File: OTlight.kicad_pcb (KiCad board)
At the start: 2 copper layers, 68 parts, among them P1 CONN_01X01, Q1 TEMT6000, Q2 Q_NMOS_GSD, T1 TRANSFO, U1 LM3478, U10 IN-14, U11 IN-14, U12 MAX6931, U13 IN-14, U14 MAX6920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

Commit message: Misakaimouto Silk + miniBiri stitch
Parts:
- removed the G*** at (47.2, 111.8)
- added G***: LOGO, OTlight:Misakaimouto, F.Cu at (47.2, 111.8)
- added REF**: Biri-Biri via, BamboulabFootprints:Biri-Biri-via-small, F.Cu at (51.8, 113.3)
- added REF**: Biri-Biri via, BamboulabFootprints:Biri-Biri-via-small, F.Cu at (89.2, 104.3)
- added REF**: Biri-Biri via, BamboulabFootprints:Biri-Biri-via-small, F.Cu at (86.4, 129.5)
- added REF**: Biri-Biri via, BamboulabFootprints:Biri-Biri-via-small, F.Cu at (91.3, 86.5)
- added REF**: Biri-Biri via, BamboulabFootprints:Biri-Biri-via-small, F.Cu at (121.3, 104.3)
- added REF**: Biri-Biri via, BamboulabFootprints:Biri-Biri-via-small, F.Cu at (118.7, 115.3)
- added REF**: Biri-Biri via, BamboulabFootprints:Biri-Biri-via-small, F.Cu at (116.6, 98.7)
- added REF**: Biri-Biri via, BamboulabFootprints:Biri-Biri-via-small, F.Cu at (60.8, 126.1)
- added REF**: Biri-Biri via, BamboulabFootprints:Biri-Biri-via-small, F.Cu at (79.0, 86.7)
- added REF**: Biri-Biri via, BamboulabFootprints:Biri-Biri-via-small, F.Cu at (57.4, 104.1)
- added REF**: Biri-Biri via, BamboulabFootprints:Biri-Biri-via-small, F.Cu at (103.4, 81.9)

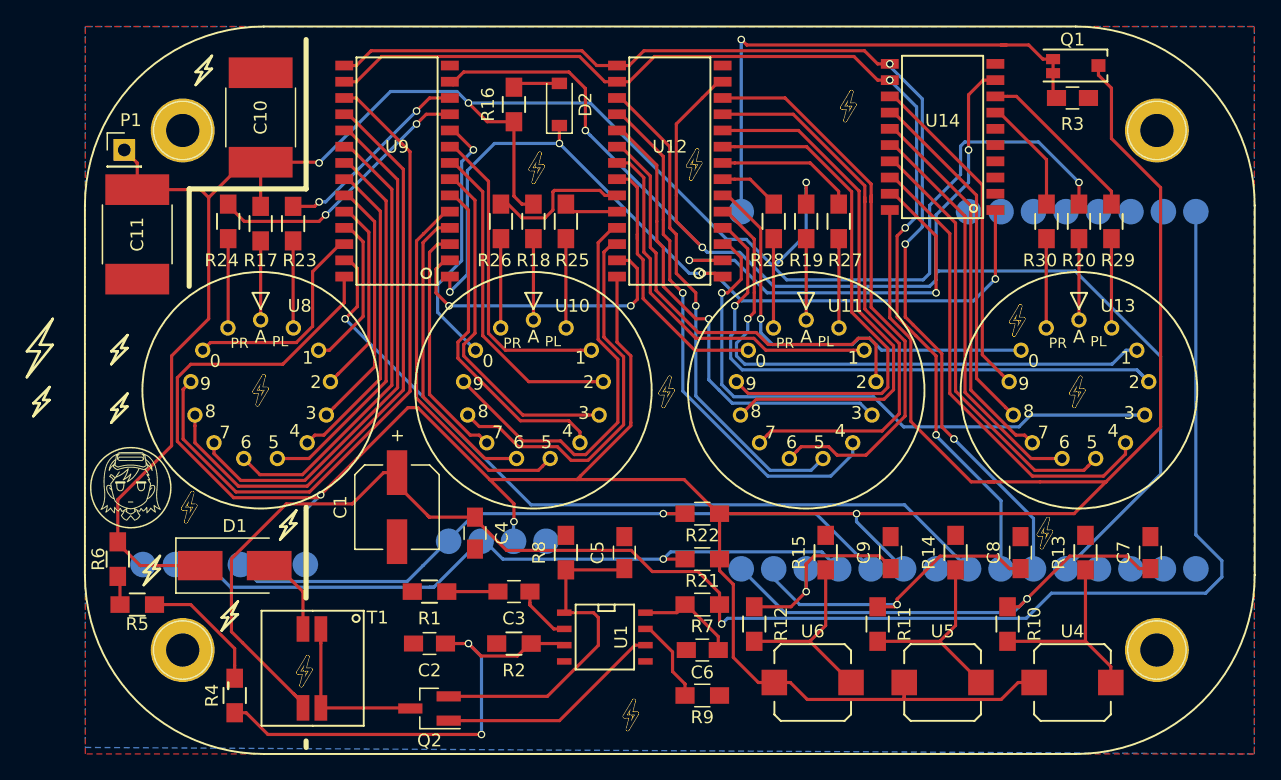
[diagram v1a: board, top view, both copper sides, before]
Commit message: Added Edgecut on top of the Altoids silkscreen
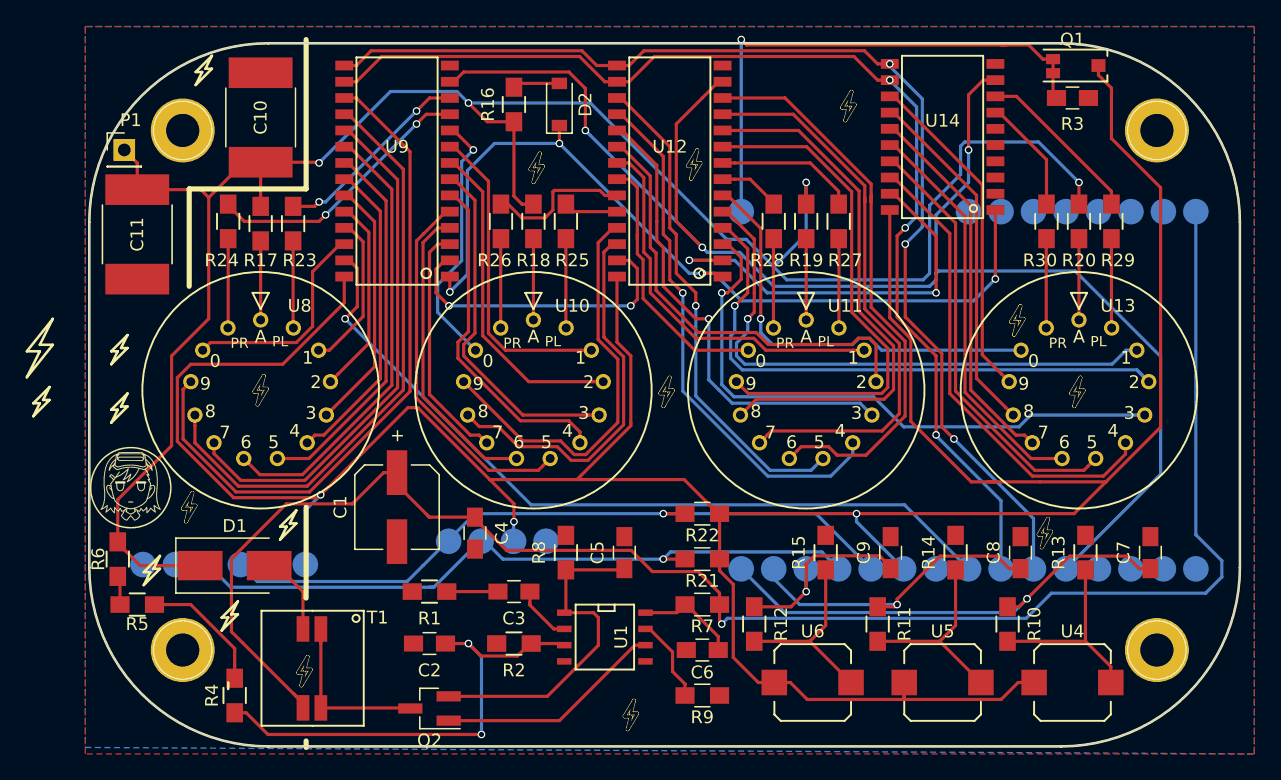
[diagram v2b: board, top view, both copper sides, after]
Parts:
- removed the REF** at (89.4, 104.1)
- moved ? 0.43 mm to (89.0, 104.0)
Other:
- board outline added: 90 x 55 mm
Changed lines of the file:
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@@
-(kicad_pcb (version 4) (host pcbnew 4.0.5)
+(kicad_pcb (version 4) (host pcbnew 4.0.6)
   (general
-    (links 0)
-    (no_connects 31)
+    (links 235)
+    (no_connects 97)
     (area 39.015999 74.51657 135.911001 132.865001)
     (thickness 1.6)
-    (drawings 57)
+    (drawings 65)
     (tracks 859)
     (zones 0)
-    (modules 79)
+    (modules 78)
     (nets 105)
   )
@@
     )
   )
-  (module BamboulabFootprints:Altoid (layer B.Cu)
-    (at 89.408 104.14)
-    (fp_text reference REF** (at 0 -5.08) (layer B.SilkS) hide
-      (effects (font (size 1 1) (thickness 0.15)) (justify mirror))
-    )
-    (fp_text value Altoid (at 0 5.08) (layer B.Fab)
-      (effects (font (size 1 1) (thickness 0.15)) (justify mirror))
-    )
-    (fp_line (start -31.75 28.45) (end 31.75 28.45) (layer B.SilkS) (width 0.15))
-    (fp_line (start -45.75 14.45) (end -45.75 -14.45) (layer B.SilkS) (width 0.15))
-    (fp_arc (start -31.75 14.45) (end -45.75 14.45) (angle -90) (layer B.SilkS) (width 0.15))
-    (fp_arc (start -31.75 -14.45) (end -45.75 -14.45) (angle 90) (layer B.SilkS) (width 0.15))
-    (fp_line (start 45.75 14.45) (end 45.75 -14.45) (layer B.SilkS) (width 0.15))
-    (fp_line (start -31.75 -28.45) (end 31.75 -28.45) (layer B.SilkS) (width 0.15))
-    (fp_arc (start 31.75 14.45) (end 31.75 28.45) (angle -90) (layer B.SilkS) (width 0.15))
-    (fp_arc (start 31.75 -14.45) (end 45.75 -14.45) (angle -90) (layer B.SilkS) (width 0.15))
-  )
-  (module BamboulabFootprints:Altoid (layer F.Cu)
-    (at 89.408 104.14)
-    (fp_text reference "" (at 0 5.08) (layer F.SilkS)
-      (effects (font (size 1 1) (thickness 0.15)))
-    )
-    (fp_text value Altoid (at 0 -5.08) (layer F.Fab)
-      (effects (font (size 1 1) (thickness 0.15)))
-    )
-    (fp_line (start -31.75 -28.45) (end 31.75 -28.45) (layer F.SilkS) (width 0.15))
-    (fp_line (start -45.75 -14.45) (end -45.75 14.45) (layer F.SilkS) (width 0.15))
-    (fp_arc (start -31.75 -14.45) (end -45.75 -14.45) (angle 90) (layer F.SilkS) (width 0.15))
-    (fp_arc (start -31.75 14.45) (end -45.75 14.45) (angle -90) (layer F.SilkS) (width 0.15))
-    (fp_line (start 45.75 -14.45) (end 45.75 14.45) (layer F.SilkS) (width 0.15))
-    (fp_line (start -31.75 28.45) (end 31.75 28.45) (layer F.SilkS) (width 0.15))
-    (fp_arc (start 31.75 -14.45) (end 31.75 -28.45) (angle 90) (layer F.SilkS) (width 0.15))
-    (fp_arc (start 31.75 14.45) (end 45.75 14.45) (angle 90) (layer F.SilkS) (width 0.15))
-  )
   (module BamboulabFootprints:SPEH120100 (layer F.Cu)
     (at 120.904 127 180)
@@
       (net 2 GND) (zone_connect 2))
   )
+  (module BamboulabFootprints:Altoid (layer F.Cu)
+    (at 89 104)
+    (fp_text reference "" (at 0 5.08) (layer F.SilkS)
+      (effects (font (size 1 1) (thickness 0.15)))
+    )
+    (fp_text value Altoid (at 0 -6) (layer F.Fab)
+      (effects (font (size 1 1) (thickness 0.15)))
+    )
+    (fp_arc (start 31 14) (end 45 14) (angle 90) (layer F.SilkS) (width 0.2))
+    (fp_line (start 45 -13) (end 45 14) (layer F.SilkS) (width 0.2))
+    (fp_line (start -31 28) (end 31 28) (layer F.SilkS) (width 0.2))
+    (fp_arc (start -31 14) (end -31 28) (angle 90) (layer F.SilkS) (width 0.2))
+    (fp_line (start -45 -13) (end -45 14) (layer F.SilkS) (width 0.2))
+    (fp_arc (start 31 -13) (end 31 -27) (angle 90) (layer F.SilkS) (width 0.2))
+    (fp_arc (start -31 -13) (end -45 -13) (angle 90) (layer F.SilkS) (width 0.2))
+    (fp_line (start -31 -27) (end 31 -27) (layer F.SilkS) (width 0.2))
+  )
+  (gr_arc (start 58 91) (end 44 91) (angle 90) (layer Edge.Cuts) (width 0.1))
+  (gr_arc (start 58 118) (end 58 132) (angle 90) (layer Edge.Cuts) (width 0.1))
+  (gr_arc (start 120 118) (end 134 118) (angle 90) (layer Edge.Cuts) (width 0.1))
+  (gr_arc (start 120 91) (end 120 77) (angle 90) (layer Edge.Cuts) (width 0.1))
+  (gr_line (start 134 118) (end 134 91) (layer Edge.Cuts) (width 0.1))
+  (gr_line (start 58 132) (end 120 132) (layer Edge.Cuts) (width 0.1))
+  (gr_line (start 44 91) (end 44 118) (layer Edge.Cuts) (width 0.1))
+  (gr_line (start 120 77) (end 58 77) (layer Edge.Cuts) (width 0.1))
   (gr_line (start 53.594 77.978) (end 53.086 78.994) (layer F.SilkS) (width 0.2))
   (gr_line (start 52.324 79.248) (end 53.594 77.978) (layer F.SilkS) (width 0.2))

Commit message: Board size to fit Altoids+ decoupling caps
NOTHING IS WHERE IT SHOULD BE
EVERYTHING IS WRONG
I AM GOING TO BED!
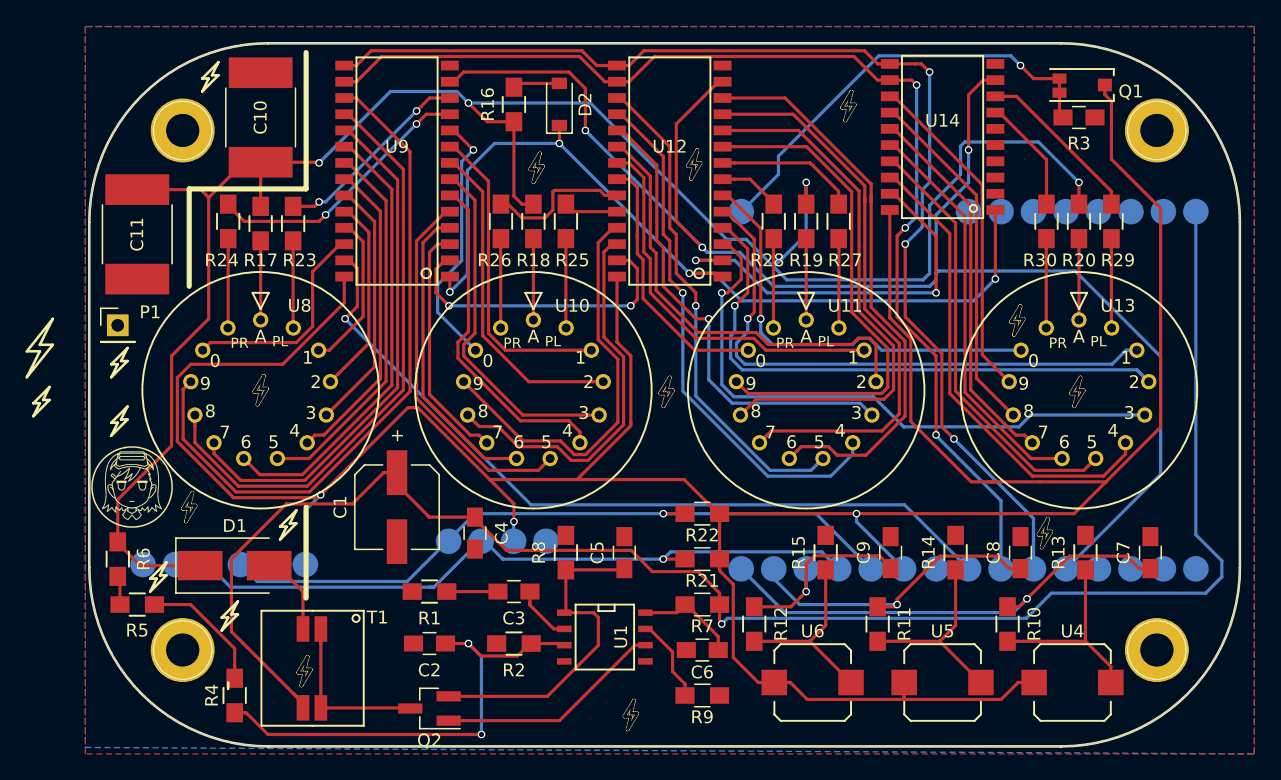
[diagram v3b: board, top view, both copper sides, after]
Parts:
- moved P1 13.7 mm to (46.2, 99.1)
- moved R3 1.61 mm to (121.4, 82.8)
- moved Q1 1.60 mm to (119.9, 80.3)
- moved G*** 0.11 mm to (47.3, 111.7)
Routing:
- net Net-(Q1-Pad2): track 42.1 -> 34.7 mm
- net /HVout: track 160.8 -> 157.3 mm
- net /CLK: track 90.1 -> 92.0 mm
- net +3V3: track 252.2 -> 250.4 mm
- net Net-(U12-Pad2): track 32.7 -> 31.7 mm
- net Net-(D2-Pad1): track 67.7 -> 68.8 mm
- net /LOAD: track 89.0 -> 90.0 mm

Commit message: Errr... as below but this time I saved first.
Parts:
- added C12: C_Small, Capacitors_SMD:C_0805_HandSoldering, F.Cu at (116.8, 90.9)
- added C13: C_Small, Capacitors_SMD:C_0805_HandSoldering, F.Cu at (80.8, 81.8)
- added C14: C_Small, Capacitors_SMD:C_0805_HandSoldering, F.Cu at (126.5, 90.9)
- added C15: C_Small, Capacitors_SMD:C_0805_HandSoldering, F.Cu at (110.7, 111.3)
- added C16: C_Small, Capacitors_SMD:C_0805_HandSoldering, F.Cu at (89.4, 111.3)
- moved D2 2.54 mm to (78.2, 81.8)
- moved R16 1.52 mm to (75.7, 81.8)
- moved REF** 0.64 mm to (79.0, 87.4)
- moved R17 0.17 mm to (57.4, 90.9)
- moved R23 0.17 mm to (59.9, 90.9)
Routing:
- net +3V3: track 250.4 -> 241.3 mm
- net Net-(C12-Pad2): track 68.8 -> 76.9 mm
- net Net-(R4-Pad1): track 10.0 -> 11.6 mm
- net Net-(D2-Pad2): track 3.68 -> 2.66 mm
- net /HVout: track 157.3 -> 156.4 mm

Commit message: Updated PCB and footprints - Changed footprints for angled pins SMD package - Repositioned holes - Locked Altoids shaped outline, holes, tubes and modules - Changed R3 for resistor package (was 0805 but as capacitor)
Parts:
- R3: footprint Capacitors_SMD:C_0805_HandSoldering -> Resistors_SMD:R_0805_HandSoldering
- U2: footprint BamboulabFootprints:NodeMCU-V2 -> BamboulabFootprints:NodeMCU-V3
- U3: footprint BamboulabFootprints:DS3231 -> BamboulabFootprints:DS3231-Angled
- U7: footprint BamboulabFootprints:BME280 -> BamboulabFootprints:BME280-Angled
- moved U7 5.18 mm to (54.9, 106.2)
- moved ? 2.59 mm to (127.0, 127.0)
- moved ? 2.56 mm to (51.0, 127.0)
- moved ? 1.89 mm to (127.0, 82.0)
- moved ? 1.85 mm to (51.0, 82.0)
- moved U2 0.79 mm to (112.0, 104.0)
- moved U3 0.44 mm to (75.7, 99.0)
- moved R3 0.10 mm to (121.5, 82.8)
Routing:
- net +5V: track 133.1 -> 63.0 mm, vias 1 -> 0
- net GND: track 2.76 -> 70.6 mm, vias 0 -> 1
- net Net-(C9-Pad1): track 16.1 -> 50.1 mm
- net /HVout: track 156.4 -> 134.7 mm, vias 4 -> 3
- net Net-(C8-Pad1): track 24.7 -> 8.04 mm, vias 1 -> 0
- net /BLANK: track 121.5 -> 106.8 mm, vias 3 -> 2
- net /CLK: track 92.0 -> 106.4 mm, vias 3 -> 4
- net Net-(C7-Pad1): track 37.7 -> 27.5 mm
- net Net-(U2-Pad12): track 0.00 -> 10.2 mm, vias 0 -> 1
- net +3V3: track 241.3 -> 246.2 mm, vias 3 -> 4
- net (no net): track 0.00 -> 2.03 mm

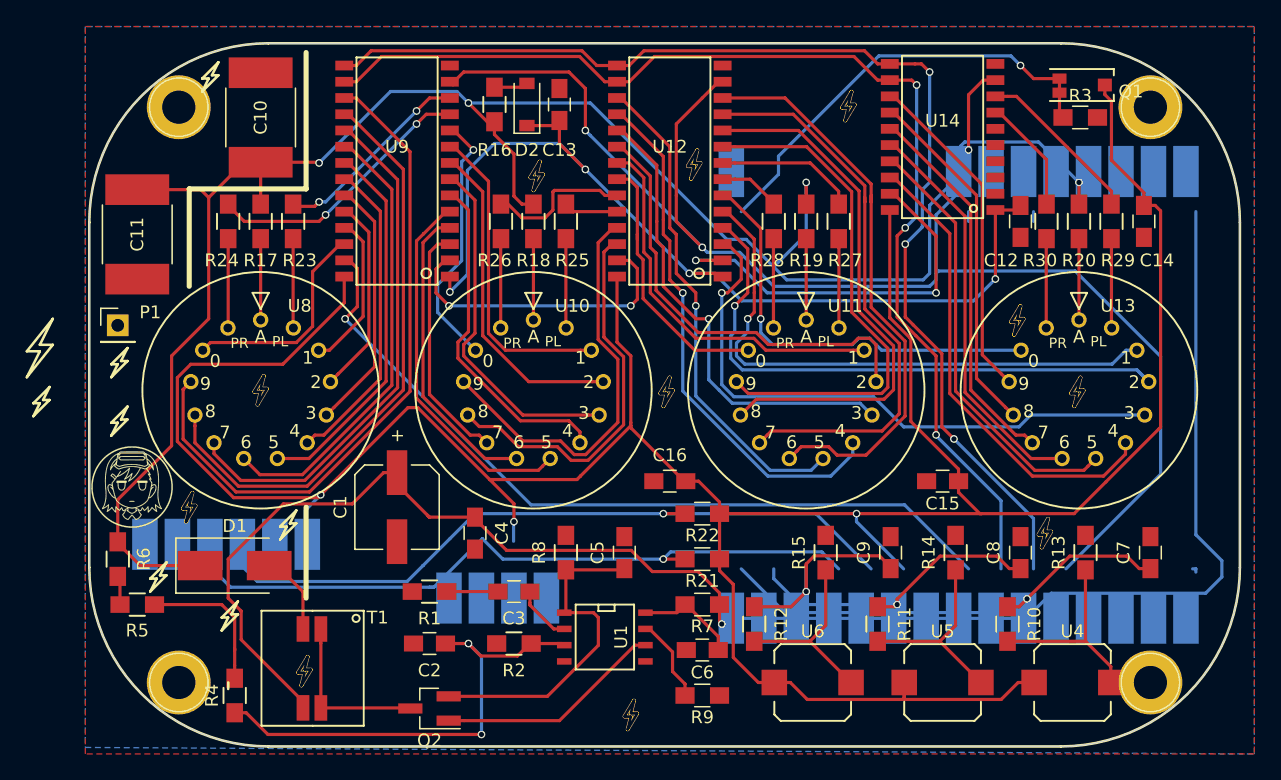
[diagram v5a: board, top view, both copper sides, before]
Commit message: Updated footprints meant reroute No unconnected traces, silk adjusted.
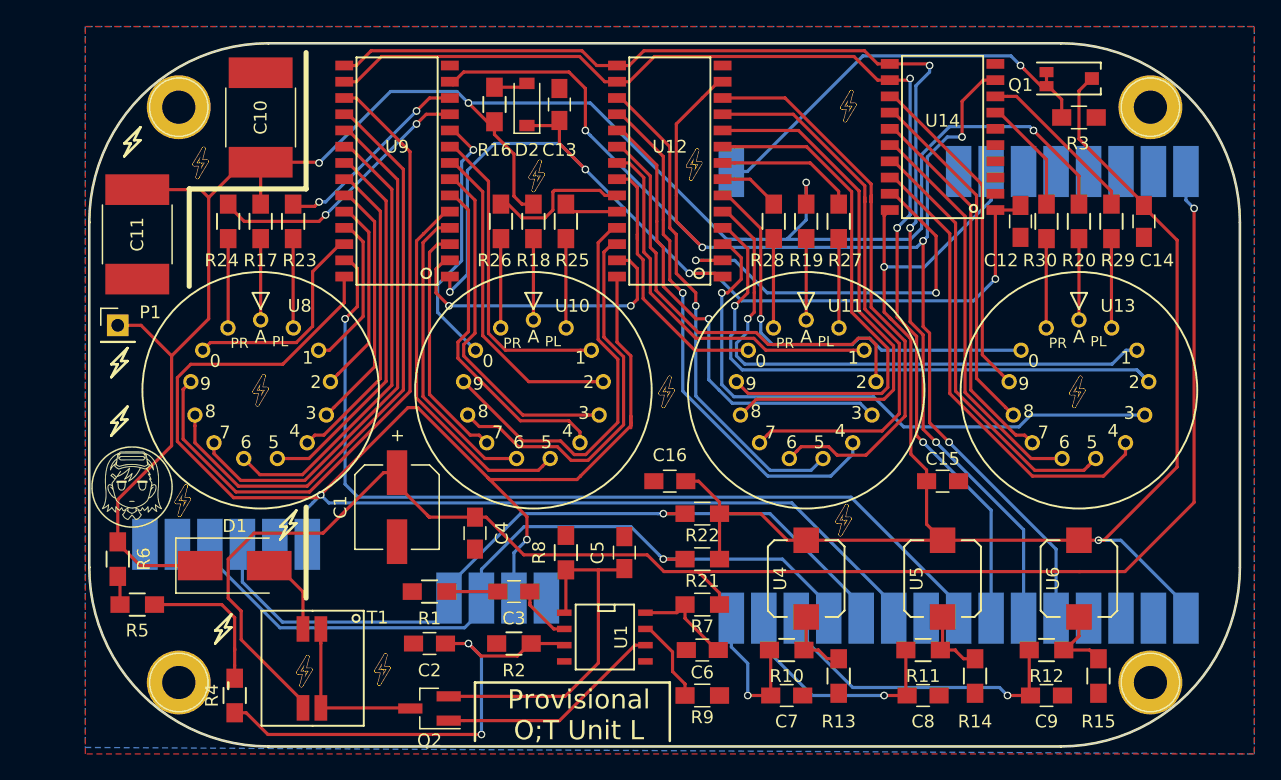
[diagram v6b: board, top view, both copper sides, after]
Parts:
- removed the REF** at (86.4, 129.5)
- removed the REF** at (118.7, 115.3)
- removed the REF** at (116.6, 98.7)
- added REF**: Biri-Biri via, BamboulabFootprints:Biri-Biri-via-small, F.Cu at (52.7, 86.4)
- added REF**: Biri-Biri via, BamboulabFootprints:Biri-Biri-via-small, F.Cu at (103.0, 114.3)
- added REF**: Biri-Biri via, BamboulabFootprints:Biri-Biri-via-small, F.Cu at (66.9, 126.0)
- moved C7 30.6 mm to (98.6, 128.0), turned to 0 degrees
- moved R15 23.4 mm to (122.9, 126.5), turned to 270 degrees
- moved R12 23.0 mm to (118.9, 124.5), turned to 0 degrees
- moved U4 22.4 mm to (100.1, 118.9), turned to 90 degrees
- moved U6 22.4 mm to (121.4, 118.9), turned to 90 degrees
- moved R13 21.6 mm to (102.6, 126.5), turned to 270 degrees
- moved R10 17.4 mm to (98.6, 124.5), turned to 0 degrees
- moved C9 16.5 mm to (118.9, 128.0), turned to 0 degrees
- moved C8 13.5 mm to (109.2, 128.0), turned to 0 degrees
- moved R14 9.77 mm to (113.3, 126.5), turned to 270 degrees
- moved U5 8.13 mm to (110.7, 118.9), turned to 90 degrees
- moved R11 4.10 mm to (109.2, 124.5), turned to 0 degrees
- moved Q1 1.14 mm to (118.9, 79.8)
- moved REF** 0.72 mm to (51.3, 112.8)
- moved R3 0.10 mm to (121.4, 82.8)
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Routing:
- net +5V: track 63.0 -> 131.0 mm, vias 0 -> 1
- net GND: track 70.6 -> 3.49 mm, vias 1 -> 0
- net +3V3: track 246.2 -> 278.8 mm
- net Net-(C9-Pad1): track 50.1 -> 25.0 mm
- net /HVout: track 134.7 -> 158.1 mm, vias 3 -> 4
- net Net-(C7-Pad1): track 27.5 -> 12.0 mm
- net Net-(C8-Pad1): track 8.04 -> 19.7 mm, vias 0 -> 1
- net /CLK: track 106.4 -> 95.6 mm, vias 4 -> 3
- net Net-(U2-Pad12): track 10.2 -> 0.00 mm, vias 1 -> 0
- net Net-(R10-Pad2): track 15.7 -> 5.66 mm
- net Net-(R11-Pad2): track 15.5 -> 5.69 mm
- net /DIN: track 62.5 -> 71.5 mm
- net Net-(R12-Pad2): track 15.0 -> 6.14 mm
- net Net-(R22-Pad2): track 55.6 -> 62.9 mm
- net Net-(R21-Pad2): track 55.3 -> 62.3 mm
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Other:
- board text added: "Provisional O;T Unit L"

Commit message: I2C footprint, silk and diode adjustments
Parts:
- P1: value CONN_01X01 -> CONN_01X02; footprint Socket_Strips:Socket_Strip_Straight_1x01_Pitch2.54mm -> Pin_Headers:Pin_Header_Straight_1x02_Pitch2.54mm
- Q2: value Q_NMOS_GSD -> RSR030N06TL
- moved REF** 7.80 mm to (49.7, 105.2)
- moved P1 6.10 mm to (46.2, 105.2), turned to 180 degrees
- moved REF** 1.28 mm to (51.4, 86.5)
- turned D2 to 270 degrees
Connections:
- D2 pad 1: Net-(C12-Pad2) -> Net-(D2-Pad1)
- D2 pad 2: Net-(D2-Pad2) -> Net-(C12-Pad2)
- R16 pad 2: Net-(D2-Pad2) -> Net-(D2-Pad1)
- U7 pad 3: Net-(R22-Pad2) -> Net-(R21-Pad2)
- U7 pad 4: Net-(R21-Pad2) -> Net-(R22-Pad2)
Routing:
- net Net-(R21-Pad2): track 62.3 -> 88.5 mm
- net /HVout: track 158.1 -> 155.1 mm
- net Net-(D2-Pad2): track 2.66 -> 0.00 mm
- net Net-(D2-Pad1): track 0.00 -> 2.66 mm
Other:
- board text added: "Pie"
- board text added: "messed"
- board text added: "up"

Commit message: Final silk adjustment. Ready for fab?
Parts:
- added G***: LOGO, OTlight:PVUnit, F.Cu at (81.8, 129.3)
- added G***: LOGO, OTlight:QR, F.Cu at (100.6, 83.3)
- added G***: LOGO, OTlight:versionNumb, F.Cu at (128.0, 122.9)
- moved REF** 7.96 mm to (95.8, 79.6)
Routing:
- net /HVout: track 155.1 -> 156.9 mm
- net Net-(C2-Pad1): track 37.7 -> 36.3 mm
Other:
- board text removed: "Pie"
- board text removed: "Provisional O;T Unit L"
- board text removed: "messed"
- board text removed: "up"
